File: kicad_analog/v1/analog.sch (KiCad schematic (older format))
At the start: 22 parts, among them P1 Conn_02x05_Odd_Even, P2 Conn_01x04, P3 Conn_01x05, P4 Conn_01x02, P5 Conn_01x01, P6 Conn_01x01, U1 TLC5620, U2 MAX9201, U3 MAX9201, U4 MCP1754-3302E_SOT89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

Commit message: Change analog switch
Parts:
- removed U5: MAX323CSA, Package_SO:SOIC-8_3.9x4.9mm_P1.27mm, symbol Analog_Switch:MAX323CSA
- added U5: TS5A3166DBVR, Package_TO_SOT_SMD:SOT-23-5, symbol Analog_Switch:TS5A3166DBVR
- JP1: value SolderJumper_2_Open -> Bypass
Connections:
- net labels removed: 75R
- wire segments 132 -> 126
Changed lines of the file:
@@
 Connection ~ 8700 6350
 Connection ~ 8350 6350
-Connection ~ 8050 6350
 Connection ~ 10450 6350
 Wire Wire Line
@@
 Wire Wire Line
 	10450 6350 10100 6350
-$Comp
-L Analog_Switch:MAX323CSA U5
-U 3 1 5DEC28BA
-P 7300 5850
-F 0 "U5" H 7480 5896 50  0000 L CNN
-F 1 "MAX323CSA" H 7480 5805 50  0000 L CNN
-F 2 "Package_SO:SOIC-8_3.9x4.9mm_P1.27mm" H 7300 5750 50  0001 C CNN
-F 3 "https://datasheets.maximintegrated.com/en/ds/MAX323-MAX325.pdf" H 7300 5850 50  0001 C CNN
-	3    7300 5850
-	1    0    0    -1
-$EndComp
-$Comp
-L Analog_Switch:MAX323CSA U5
-U 2 1 5DEC1522
-P 2550 3050
-F 0 "U5" V 2596 3180 50  0000 L CNN
-F 1 "MAX323CSA" V 2505 3180 50  0000 L CNN
-F 2 "Package_SO:SOIC-8_3.9x4.9mm_P1.27mm" H 2550 2950 50  0001 C CNN
-F 3 "https://datasheets.maximintegrated.com/en/ds/MAX323-MAX325.pdf" H 2550 3050 50  0001 C CNN
-	2    2550 3050
-	0    1    -1   0
-$EndComp
-$Comp
-L Analog_Switch:MAX323CSA U5
-U 1 1 5DEC049D
-P 1750 3050
-F 0 "U5" V 1704 3179 50  0000 L CNN
-F 1 "MAX323CSA" V 1795 3179 50  0000 L CNN
-F 2 "Package_SO:SOIC-8_3.9x4.9mm_P1.27mm" H 1750 2950 50  0001 C CNN
-F 3 "https://datasheets.maximintegrated.com/en/ds/MAX323-MAX325.pdf" H 1750 3050 50  0001 C CNN
-	1    1750 3050
-	0    -1   1    0
-$EndComp
 Wire Wire Line
 	2400 5600 2400 5700
@@
 Wire Wire Line
 	8050 5650 8350 5650
-Connection ~ 8050 5650
 Text Label 7900 5650 2    50   ~ 0
 VCC
@@
 $EndComp
 Wire Wire Line
-	7550 5650 7550 5350
-Wire Wire Line
-	7550 5350 7300 5350
-Wire Wire Line
-	7300 6350 8050 6350
-Wire Wire Line
-	7550 5650 8050 5650
-Wire Wire Line
-	1750 2750 2550 2750
-Connection ~ 1750 3350
-Wire Wire Line
-	1750 3350 2550 3350
-Wire Wire Line
-	1750 2750 1750 1900
-Wire Wire Line
-	1750 1900 1900 1900
-Connection ~ 1750 2750
-Wire Wire Line
 	1900 1900 1900 1950
 Wire Wire Line
-	1150 3350 1750 3350
-Wire Wire Line
-	1950 3050 2150 3050
-Wire Wire Line
-	2150 3050 2150 4650
-Wire Wire Line
-	2150 4650 3500 4650
-Wire Wire Line
-	3500 4650 3500 5600
-Wire Wire Line
 	3500 5600 3400 5600
-Connection ~ 2150 3050
-Wire Wire Line
-	2150 3050 2350 3050
 $Comp
 L Jumper:SolderJumper_2_Open JP1
@@
 P 1900 2100
 F 0 "JP1" V 1854 2168 50  0000 L CNN
-F 1 "SolderJumper_2_Open" V 1900 900 50  0000 L CNN
+F 1 "Bypass" H 1800 1950 50  0000 L CNN
 F 2 "Jumper:SolderJumper-2_P1.3mm_Open_RoundedPad1.0x1.5mm" H 1900 2100 50  0001 C CNN
 F 3 "~" H 1900 2100 50  0001 C CNN
@@
 	6850 5300 3900 5300
 Connection ~ 3900 5300
-Text Label 2600 4650 0    50   ~ 0
-TERMINATE
-Text Label 2050 2750 0    50   ~ 0
-75R
 Connection ~ 1900 2250
 Wire Wire Line
 	1900 2250 1900 2350
-Wire Wire Line
-	1150 3350 1150 2350
-Wire Wire Line
-	1150 2350 1600 2350
-Connection ~ 1600 2350
 Wire Wire Line
 	1700 1200 1900 1200
@@
 Wire Wire Line
 	2200 1200 3450 1200
+$Comp
+L Analog_Switch:TS5A3166DBVR U5
+U 1 1 5DD31595
+P 1600 3250
+F 0 "U5" H 800 3450 50  0000 C CNN
+F 1 "TS5A3166DBVR" H 800 3350 50  0000 C CNN
+F 2 "Package_TO_SOT_SMD:SOT-23-5" H 1550 3100 50  0001 C CNN
+F 3 " http://www.ti.com/lit/ds/symlink/ts5a3166.pdf" H 1600 3350 50  0001 C CNN
+	1    1600 3250
+	-1   0    0    -1
+$EndComp
+Wire Wire Line
+	7900 5650 8050 5650
+Connection ~ 8050 5650
+Wire Wire Line
+	8050 6350 7900 6350
+Connection ~ 8050 6350
+Wire Wire Line
+	1900 3250 1900 2350
+Wire Wire Line
+	1200 1900 1200 3250
+Wire Wire Line
+	1200 3250 1300 3250
+Wire Wire Line
+	1200 1900 1900 1900
+Wire Wire Line
+	2150 3350 1900 3350
+Wire Wire Line
+	2150 4650 2150 3350
+Text Label 2600 4650 0    50   ~ 0
+TERMINATE
+Wire Wire Line
+	3500 4650 3500 5600
+Wire Wire Line
+	2150 4650 3500 4650
+Text Label 1500 3550 3    50   ~ 0
+GND
+Text Label 1500 2950 1    50   ~ 0
+VCC
 $EndSCHEMATC

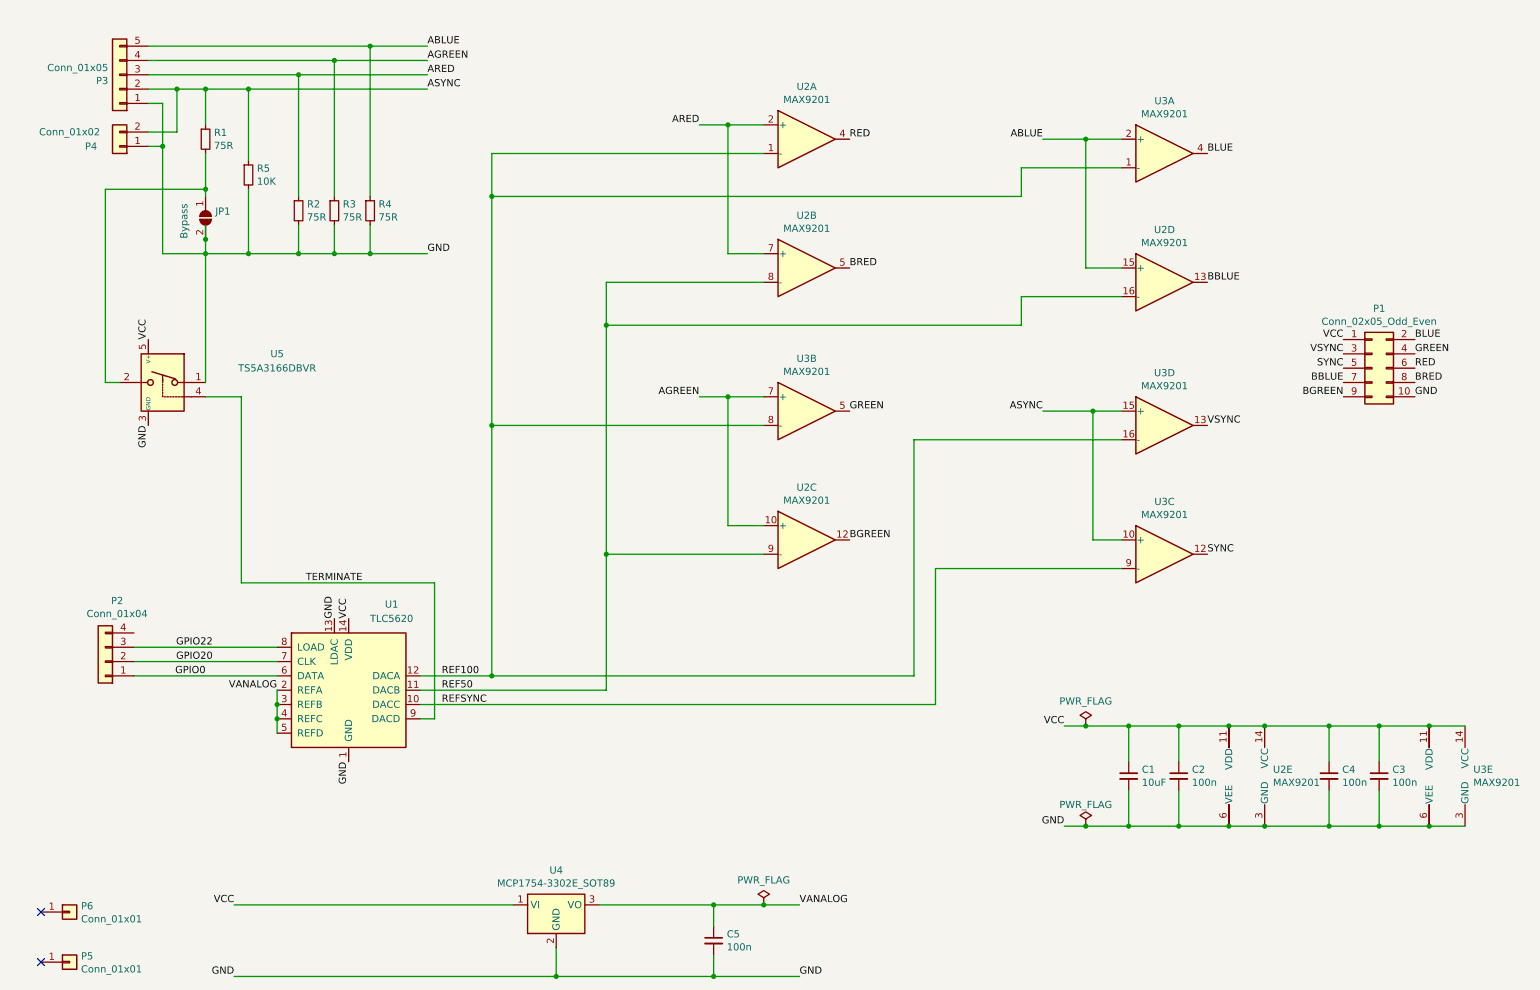
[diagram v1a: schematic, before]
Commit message: Add second DAC footprint and change regulator
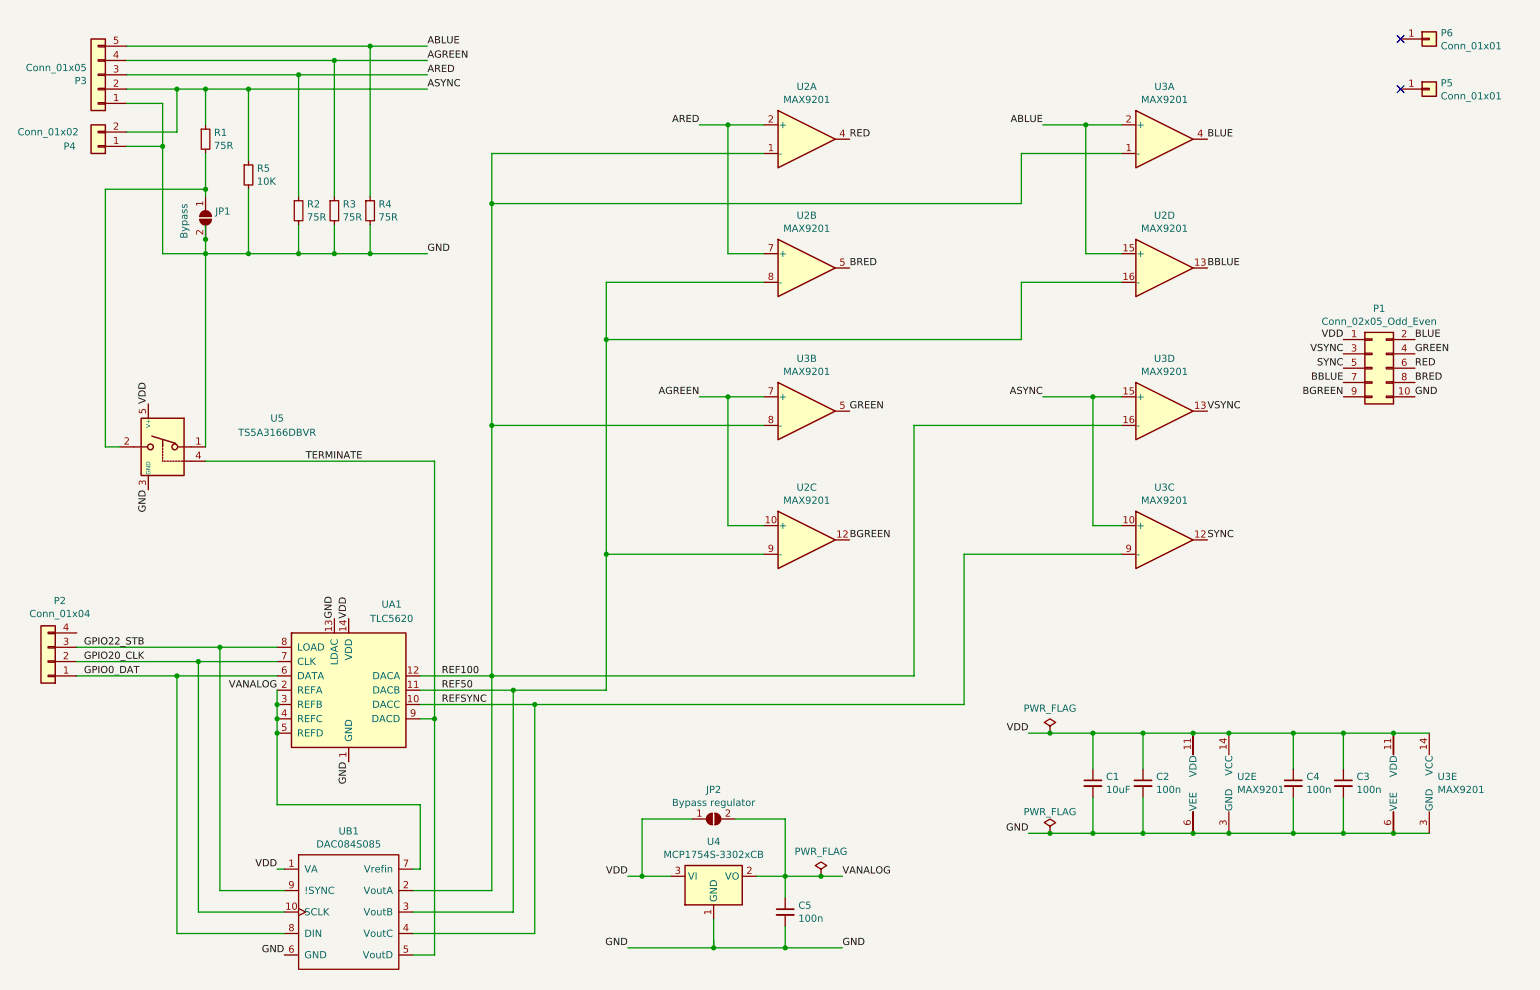
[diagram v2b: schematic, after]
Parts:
- removed U4: MCP1754-3302E_SOT89, Package_TO_SOT_SMD:SOT-89-3, symbol Regulator_Linear:MCP1754-3302E_SOT89
- added JP2: Bypass regulator, Jumper:SolderJumper-2_P1.3mm_Open_RoundedPad1.0x1.5mm, symbol Jumper:SolderJumper_2_Open
- added U4: MCP1754S-3302xCB, Package_TO_SOT_SMD:SOT-23_Handsoldering, symbol Regulator_Linear:MCP1754S-3302xCB
- added UB1: DAC084S085, Package_SO:VSSOP-10_3x3mm_P0.5mm, symbol DAC084S085:DAC084S085
- U5: footprint Package_TO_SOT_SMD:SOT-23-5 -> Package_TO_SOT_SMD:SOT-23-5_HandSoldering
- renumbered U1 to UA1
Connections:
- net GND: now also U4.1 (GND), UB1.6 (GND)
- net REF100: now also UB1.2 (VoutA)
- net REF50: now also UB1.3 (VoutB)
- net REFSYNC: now also UB1.4 (VoutC)
- net TERMINATE: now also UB1.5 (VoutD)
- net VANALOG: now also JP2.2 (B), U4.2 (VO), UB1.7 (Vrefin)
- net GPIO0 renamed GPIO0_DAT
- net GPIO0_DAT: now also UB1.8 (DIN)
- net GPIO20 renamed GPIO20_CLK
- net GPIO20_CLK: now also UB1.10 (SCLK)
- net GPIO22 renamed GPIO22_STB
- net GPIO22_STB: now also UB1.9 (!SYNC)
- net VCC renamed VDD
- net VDD: now also JP2.1 (A), U4.3 (VI), UB1.1 (VA)
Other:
- moved on the sheet: C1, C2, C3, C4, C5, P2, P3, P4, P5, P6, U2D, U2E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

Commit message: Add more config jumpers
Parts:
- added JP3: SolderJumper_3_Bridged12, Jumper:SolderJumper-3_P1.3mm_Bridged12_RoundedPad1.0x1.5mm, symbol Jumper:SolderJumper_3_Bridged12
- renumbered P5 to P7
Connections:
- net VANALOG: now also JP3.1 (A)
- net GPIO20_CLK renamed GPIO1_CLK
- net VDD renamed VCC
- net VCC: now also JP3.3 (B); no longer U5.5 (V+)
- new net: JP3.2 (C), U5.5 (V+)
- no-connect marks 2 -> 3
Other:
- note added: "NOTE: Connections\nreversed compared\nto RGB to HD pcb"
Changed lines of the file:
@@
 $EndDescr
 Text Label 4850 6700 2    50   ~ 0
-VDD
+VCC
 Text Label 6350 6700 0    50   ~ 0
 VANALOG
@@
 $EndComp
 $Comp
-L Connector_Generic:Conn_01x01 P5
+L Connector_Generic:Conn_01x01 P7
 U 1 1 5DD08736
 P 10450 1200
-F 0 "P5" H 10530 1242 50  0000 L CNN
+F 0 "P7" H 10530 1242 50  0000 L CNN
 F 1 "Conn_01x01" H 10530 1151 50  0000 L CNN
 F 2 "Connector_PinHeader_2.54mm:PinHeader_1x01_P2.54mm_Vertical" H 10450 1200 50  0001 C CNN
@@
 $EndComp
 Text Label 2900 4900 1    50   ~ 0
-VDD
+VCC
 $Comp
 L Connector_Generic:Conn_01x04 P2
@@
 	7800 5700 8100 5700
 Text Label 7650 5700 2    50   ~ 0
-VDD
+VCC
 Connection ~ 8800 5700
 Wire Wire Line
@@
 GPIO0_DAT
 Text Label 1050 5200 0    50   ~ 0
-GPIO20_CLK
+GPIO1_CLK
 Text Label 1050 5100 0    50   ~ 0
 GPIO22_STB
@@
 GND
 Text Label 9850 2950 2    50   ~ 0
-VDD
+VCC
 Text Label 8900 2450 0    50   ~ 0
 BBLUE
@@
 Text Label 1500 4000 3    50   ~ 0
 GND
-Text Label 1500 3400 1    50   ~ 0
-VDD
 $Comp
 L DAC084S085:DAC084S085 UB1
@@
 Wire Wire Line
 	3500 7250 3500 5600
-Connection ~ 3500 5600
 Wire Wire Line
 	3350 6650 3400 6650
@@
 GND
 Text Label 2400 6650 2    50   ~ 0
-VDD
+VCC
 $Comp
 L Regulator_Linear:MCP1754S-3302xCB U4
@@
 Wire Wire Line
 	5950 6300 5950 6700
-Wire Wire Line
-	3500 3800 3500 5600
-Text Label 2600 3800 0    50   ~ 0
+Text Label 2100 3800 0    50   ~ 0
 TERMINATE
-Wire Wire Line
-	1900 3800 3500 3800
 Wire Wire Line
 	3900 1650 3900 2000
@@
 Wire Wire Line
 	4700 2950 4700 4450
+NoConn ~ 1000 5000
+Text Notes 9800 3800 0    50   ~ 0
+NOTE: Connections\nreversed compared\nto RGB to HD pcb
+Text Label 2600 3000 2    50   ~ 0
+VANALOG
+Text Label 3000 3000 0    50   ~ 0
+VCC
+Wire Wire Line
+	2800 3150 2800 3300
+Wire Wire Line
+	2800 3300 1500 3300
+Wire Wire Line
+	1500 3300 1500 3400
+Connection ~ 3500 5600
+Wire Wire Line
+	1900 3800 3500 3800
+Wire Wire Line
+	3500 3800 3500 5600
+$Comp
+L Jumper:SolderJumper_3_Bridged12 JP3
+U 1 1 5DD334FB
+P 2800 3000
+F 0 "JP3" H 2800 3205 50  0000 C CNN
+F 1 "SolderJumper_3_Bridged12" H 2800 3114 50  0000 C CNN
+F 2 "Jumper:SolderJumper-3_P1.3mm_Bridged12_RoundedPad1.0x1.5mm" H 2800 3000 50  0001 C CNN
+F 3 "~" H 2800 3000 50  0001 C CNN
+	1    2800 3000
+	1    0    0    -1
+$EndComp
 $EndSCHEMATC

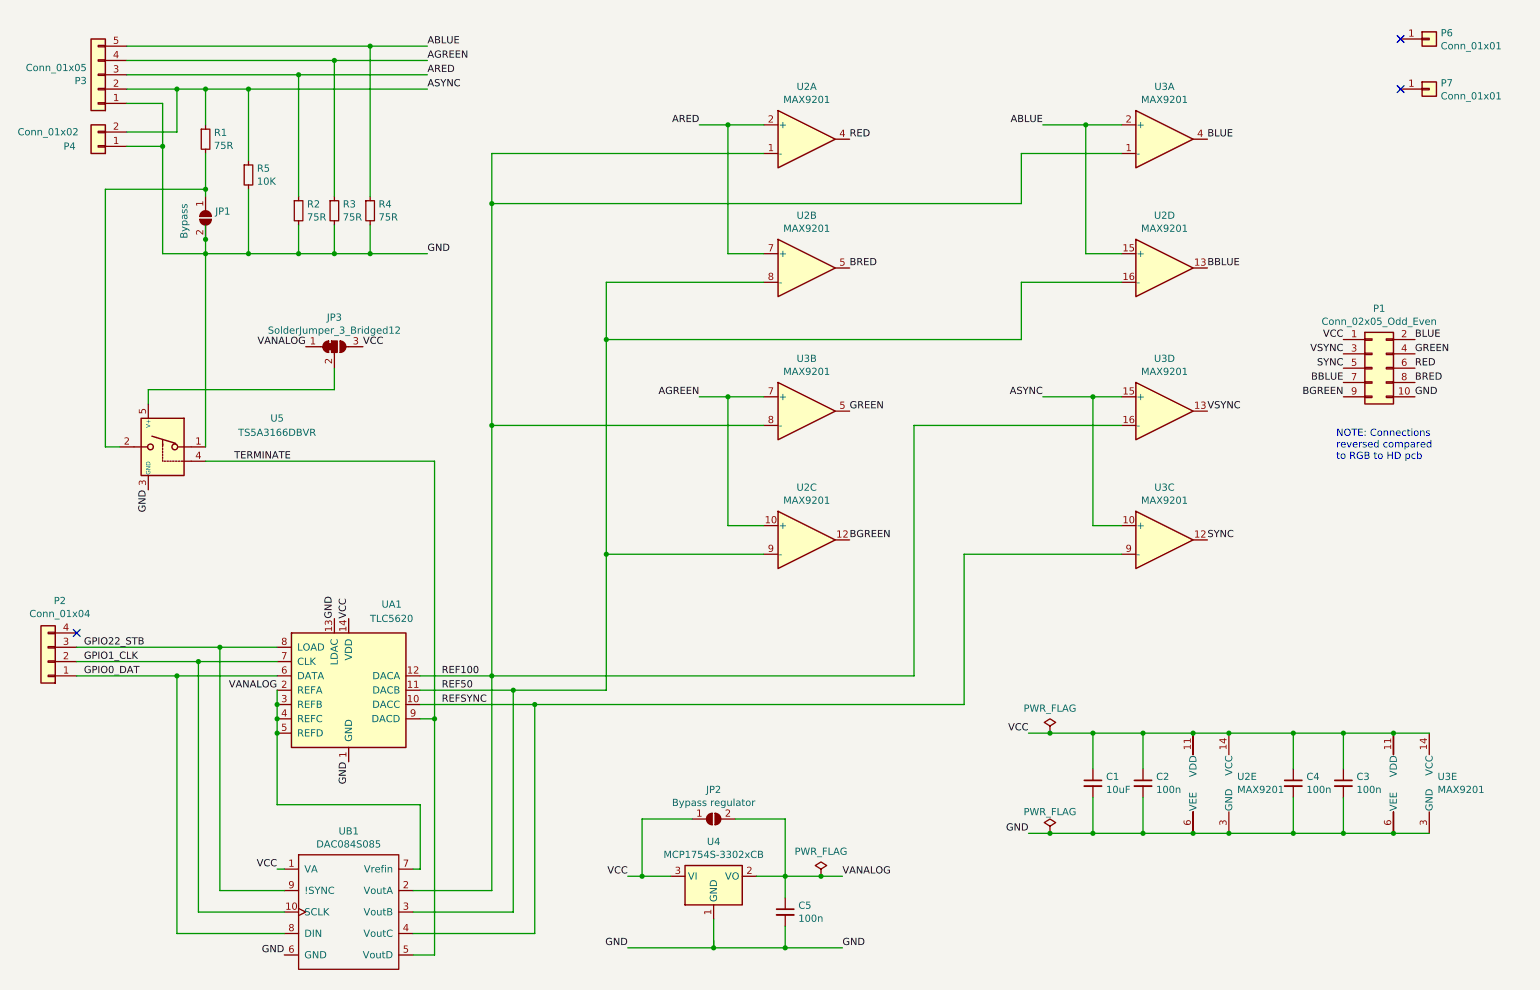
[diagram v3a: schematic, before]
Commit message: Move RGB socket
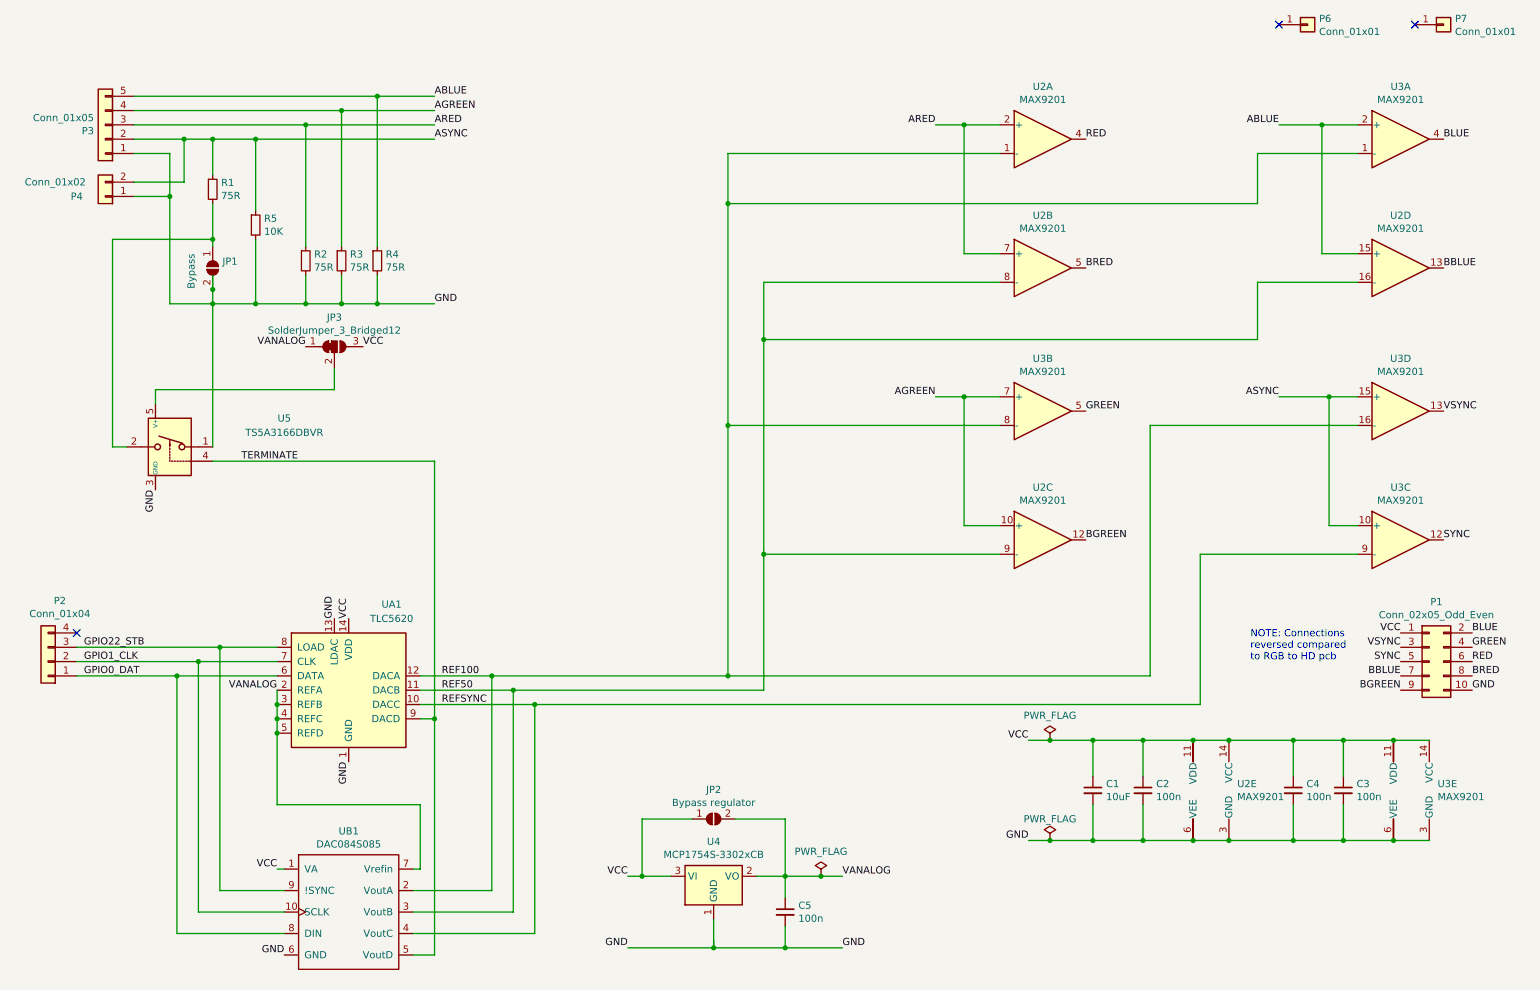
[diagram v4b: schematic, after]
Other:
- moved on the sheet: C1, C2, C3, C4, JP1, P1, P3, P4, P6, P7, R1, R2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
